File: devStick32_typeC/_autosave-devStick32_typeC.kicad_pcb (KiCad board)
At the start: 2 copper layers, 35.6 x 82.6 mm, 9 parts, among them J1 Conn_01x06_Male, J2 Conn_01x14_Male, J3 Conn_01x14_Male, J4 Conn_02x05_Odd_Even, J5 CX70M-24P1

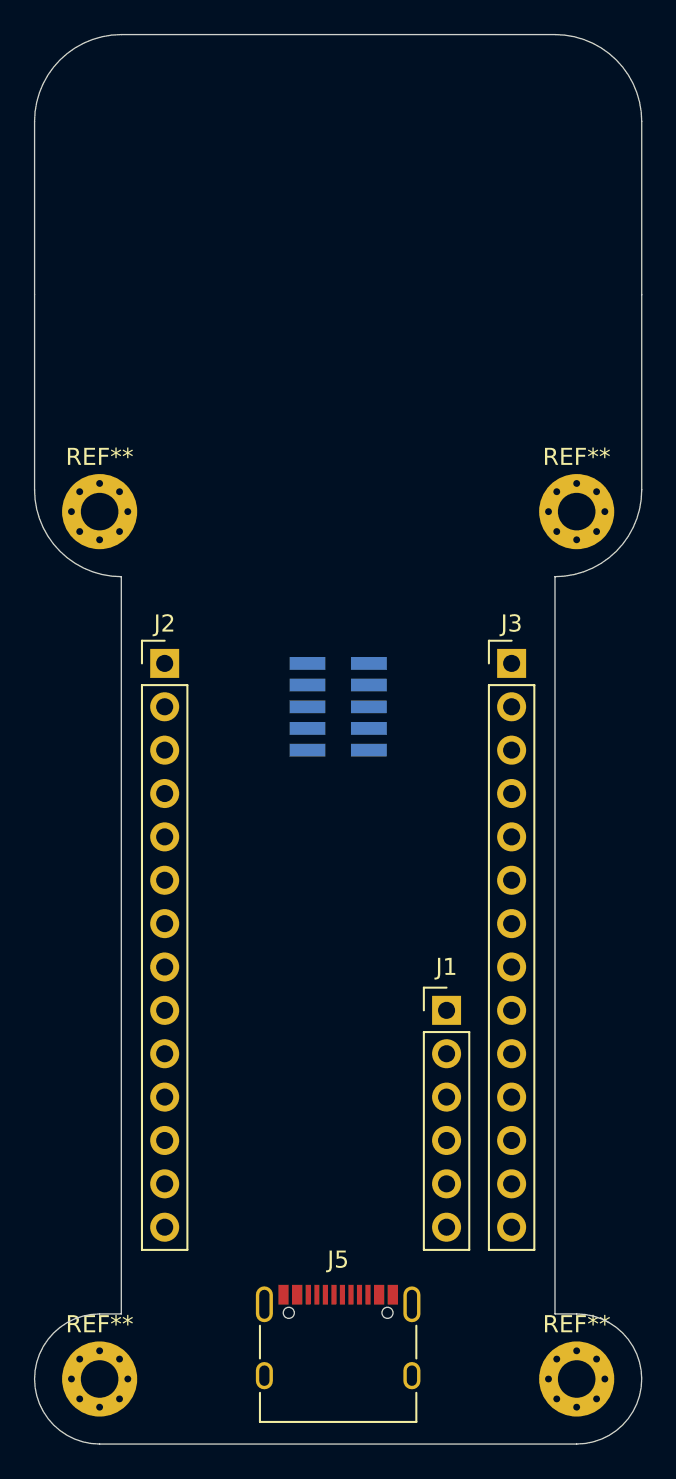
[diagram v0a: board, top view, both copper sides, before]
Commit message: Added ESP32-D0 on schema and PCB
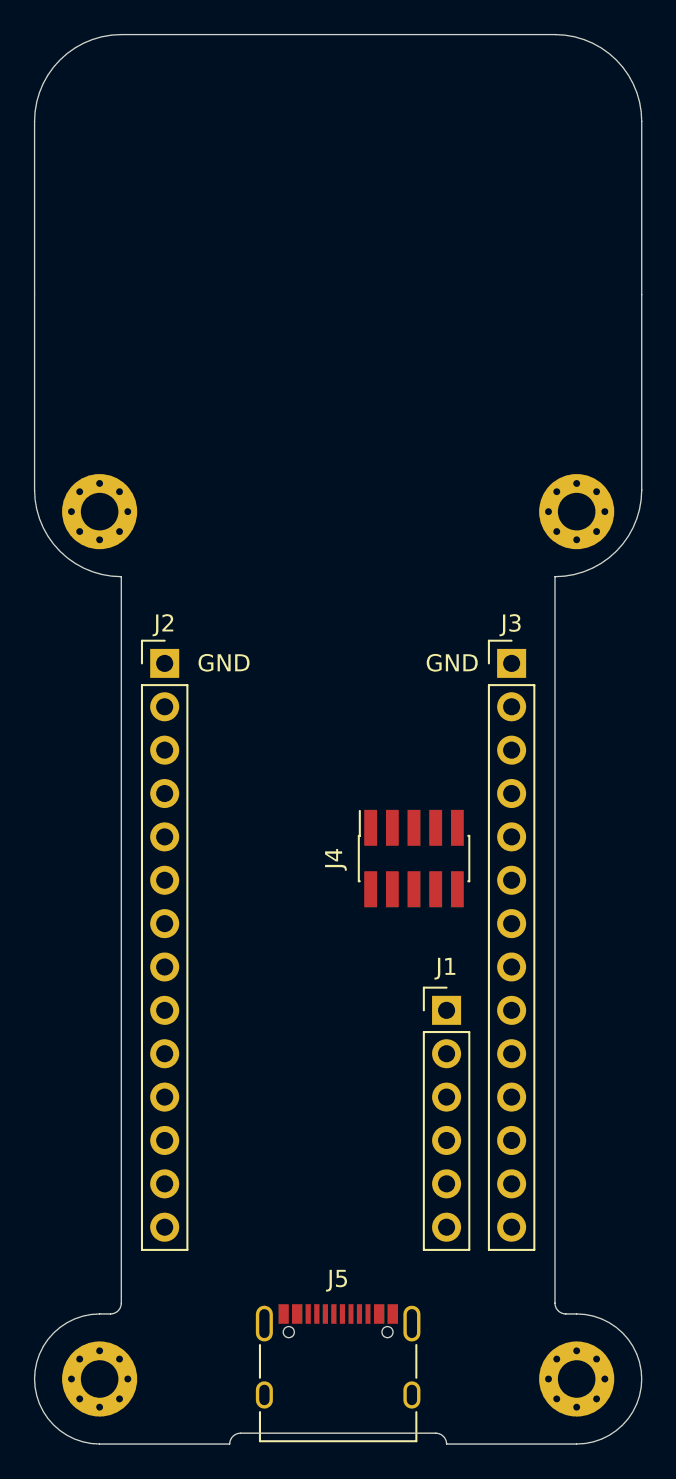
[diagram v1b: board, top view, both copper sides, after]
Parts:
- J4: moved to F.Cu
- moved J4 9.94 mm to (164.5, 95.2), turned to 90 degrees
- moved J5 1.13 mm to (160.0, 125.6)
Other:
- outline, holes or cut-outs redrawn
- board text added: "GND"
